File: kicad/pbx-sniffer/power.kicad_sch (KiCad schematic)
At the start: 0 parts

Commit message: add external power circuitry for mcu
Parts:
- added C1: 10u, Capacitor_SMD:C_0603_1608Metric, symbol Device:C_Small
- added C10, C11, C14, C16: 1u, symbol Device:C_Small
- added C12, C13, C15, C17, C18, C19, C3, C4, C5, C6, C7: 100n, symbol Device:C_Small
- added C2: 22u, Capacitor_SMD:C_0603_1608Metric, symbol Device:C_Small
- added C20, C8, C9: 4.7u, symbol Device:C_Small
- added D1: LED_Small, LED_SMD:LED_0805_2012Metric, symbol Device:LED_Small
- added J49: USB_C_Receptacle_USB2.0_14P, Connector_USB:USB_C_Receptacle_GCT_USB4125-xx-x_6P_TopMnt_Horizontal, symbol Connector:USB_C_Receptacle_USB2.0_14P
- added R1: 200, Resistor_SMD:R_0402_1005Metric, symbol Device:R
- added U2: AZ1117CH2-3.3, Package_TO_SOT_SMD:TO-252-2, symbol Regulator_Linear:AZ1117CH2-3.3
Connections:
- new net: D1.2 (A), R1.2
- new net +3V3: C10.1, C11.1, C12.1, C13.1, C14.1, C15.1, C16.1, C17.1, C18.1, C19.1, C2.1, C20.1, C3.1, C4.1, C5.1, C6.1, C7.1, C8.1, R1.1, U2.3 (OUT)
- new net +5V: C1.1, C9.1, J49.A4 (VBUS), J49.A9 (VBUS), J49.B4 (VBUS), J49.B9 (VBUS), U2.1 (IN)
- new net GND: C1.2, C10.2, C11.2, C12.2, C13.2, C14.2, C15.2, C16.2, C17.2, C18.2, C19.2, C2.2, C20.2, C8.2, C9.2, D1.1 (K), J49.A1 (GND), J49.A12 (GND), J49.B1 (GND), J49.B12 (GND), J49.S1 (SHIELD), U2.2 (GND)
- no-connect marks 0 -> 6
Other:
- note added: "3V3 Regulator"
- note added: "MCU USB External Components"
- note added: "MCU VDD External Components"
- note added: "MCU VDDA/VBAT External Components"
- note added: "MCU VDDXSPI1 External Components"
- note added: "USB C Power Input (5V 1A)"

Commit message: add footprints and part numbers for power caps
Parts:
- C10, C11, C14, C16: footprint (none) -> Capacitor_SMD:C_0603_1608Metric; DKPN (none) -> 1276-1946-1-ND
- C12, C13, C15, C17, C18, C19, C3, C4, C5, C6, C7: footprint (none) -> Capacitor_SMD:C_0402_1005Metric; DKPN (none) -> 1276-1043-1-ND
- C20, C8, C9: footprint (none) -> Capacitor_SMD:C_0603_1608Metric; DKPN (none) -> 1276-1044-1-ND
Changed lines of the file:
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@@
 		(rev "v0.1")
 		(company "M5")
-		(comment 4 "Tobe Cynar")
+		(comment 4 "Tobe Cynar, Ian Butler")
+		(comment 5 "Ian Butler")
 	)
 	(rectangle
@@
 			)
 		)
-		(property "Footprint" ""
+		(property "Footprint" "Capacitor_SMD:C_0402_1005Metric"
 			(at 109.22 107.95 0)
 			(effects
@@
 			)
 		)
+		(property "DKPN" "1276-1043-1-ND"
+			(at 109.22 107.95 0)
+			(effects
+				(font
+					(size 1.27 1.27)
+				)
+				(hide yes)
+			)
+		)
 		(pin "1"
 		)
@@
 			)
 		)
-		(property "Footprint" ""
+		(property "Footprint" "Capacitor_SMD:C_0603_1608Metric"
 			(at 64.77 102.87 0)
 			(effects
@@
 			)
 		)
+		(property "DKPN" "1276-1946-1-ND"
+			(at 64.77 102.87 0)
+			(effects
+				(font
+					(size 1.27 1.27)
+				)
+				(hide yes)
+			)
+		)
 		(pin "2"
 		)
@@
 			)
 		)
-		(property "Footprint" ""
+		(property "Footprint" "Capacitor_SMD:C_0603_1608Metric"
 			(at 34.29 102.87 0)
 			(effects
@@
 			)
 		)
+		(property "DKPN" "1276-1946-1-ND"
+			(at 34.29 102.87 0)
+			(effects
+				(font
+					(size 1.27 1.27)
+				)
+				(hide yes)
+			)
+		)
 		(pin "2"
 		)
@@
 			)
 		)
-		(property "Footprint" ""
+		(property "Footprint" "Capacitor_SMD:C_0603_1608Metric"
 			(at 152.4 109.22 0)
 			(effects
@@
 			)
 		)
+		(property "DKPN" "1276-1044-1-ND"
+			(at 152.4 109.22 0)
+			(effects
+				(font
+					(size 1.27 1.27)
+				)
+				(hide yes)
+			)
+		)
 		(pin "2"
 		)
@@
 			)
 		)
-		(property "Footprint" ""
+		(property "Footprint" "Capacitor_SMD:C_0402_1005Metric"
 			(at 55.88 102.87 0)
 			(effects
@@
 			)
 		)
+		(property "DKPN" "1276-1043-1-ND"
+			(at 55.88 102.87 0)
+			(effects
+				(font
+					(size 1.27 1.27)
+				)
+				(hide yes)
+			)
+		)
 		(pin "1"
 		)
@@
 			)
 		)
-		(property "Footprint" ""
+		(property "Footprint" "Capacitor_SMD:C_0402_1005Metric"
 			(at 25.4 138.43 0)
 			(effects
@@
 			)
 		)
+		(property "DKPN" "1276-1043-1-ND"
+			(at 25.4 138.43 0)
+			(effects
+				(font
+					(size 1.27 1.27)
+				)
+				(hide yes)
+			)
+		)
 		(pin "1"
 		)
@@
 			)
 		)
-		(property "Footprint" ""
+		(property "Footprint" "Capacitor_SMD:C_0603_1608Metric"
 			(at 118.11 107.95 0)
 			(effects
@@
 			)
 		)
+		(property "DKPN" "1276-1946-1-ND"
+			(at 118.11 107.95 0)
+			(effects
+				(font
+					(size 1.27 1.27)
+				)
+				(hide yes)
+			)
+		)
 		(pin "2"
 		)
@@
 			)
 		)
-		(property "Footprint" ""
+		(property "Footprint" "Capacitor_SMD:C_0402_1005Metric"
 			(at 43.18 138.43 0)
 			(effects
@@
 			)
 		)
+		(property "DKPN" "1276-1043-1-ND"
+			(at 43.18 138.43 0)
+			(effects
+				(font
+					(size 1.27 1.27)
+				)
+				(hide yes)
+			)
+		)
 		(pin "1"
 		)
@@
 			)
 		)
-		(property "Footprint" ""
+		(property "Footprint" "Capacitor_SMD:C_0402_1005Metric"
 			(at 133.35 72.39 0)
 			(effects
@@
 			)
 		)
+		(property "DKPN" "1276-1043-1-ND"
+			(at 133.35 72.39 0)
+			(effects
+				(font
+					(size 1.27 1.27)
+				)
+				(hide yes)
+			)
+		)
 		(pin "1"
 		)
@@
 			)
 		)
-		(property "Footprint" ""
+		(property "Footprint" "Capacitor_SMD:C_0603_1608Metric"
 			(at 125.73 107.95 0)
 			(effects
@@
 			)
 		)
+		(property "DKPN" "1276-1946-1-ND"
+			(at 125.73 107.95 0)
+			(effects
+				(font
+					(size 1.27 1.27)
+				)
+				(hide yes)
+			)
+		)
 		(pin "2"
 		)
@@
 			)
 		)
-		(property "Footprint" ""
+		(property "Footprint" "Capacitor_SMD:C_0402_1005Metric"
 			(at 115.57 72.39 0)
 			(effects
@@
 			)
 		)
+		(property "DKPN" "1276-1043-1-ND"
+			(at 115.57 72.39 0)
+			(effects
+				(font
+					(size 1.27 1.27)
+				)
+				(hide yes)
+			)
+		)
 		(pin "1"
 		)
@@
 			)
 		)
-		(property "Footprint" ""
+		(property "Footprint" "Capacitor_SMD:C_0402_1005Metric"
 			(at 106.68 72.39 0)
 			(effects
@@
 			)
 		)
+		(property "DKPN" "1276-1043-1-ND"
+			(at 106.68 72.39 0)
+			(effects
+				(font
+					(size 1.27 1.27)
+				)
+				(hide yes)
+			)
+		)
 		(pin "1"
 		)
@@
 			)
 		)
-		(property "Footprint" ""
+		(property "Footprint" "Capacitor_SMD:C_0402_1005Metric"
 			(at 34.29 138.43 0)
 			(effects
@@
 			)
 		)
+		(property "DKPN" "1276-1043-1-ND"
+			(at 34.29 138.43 0)
+			(effects
+				(font
+					(size 1.27 1.27)
+				)
+				(hide yes)
+			)
+		)
 		(pin "1"
 		)
@@
 			)
 		)
-		(property "Footprint" ""
+		(property "Footprint" "Capacitor_SMD:C_0402_1005Metric"
 			(at 124.46 72.39 0)
 			(effects
@@
 			)
 		)
+		(property "DKPN" "1276-1043-1-ND"
+			(at 124.46 72.39 0)
+			(effects
+				(font
+					(size 1.27 1.27)
+				)
+				(hide yes)
+			)
+		)
 		(pin "1"
 		)
@@
 			)
 		)
-		(property "Footprint" ""
+		(property "Footprint" "Capacitor_SMD:C_0603_1608Metric"
 			(at 151.13 72.39 0)
 			(effects
@@
 			)
 		)
+		(property "DKPN" "1276-1044-1-ND"
+			(at 151.13 72.39 0)
+			(effects
+				(font
+					(size 1.27 1.27)
+				)
+				(hide yes)
+			)
+		)
 		(pin "2"
 		)
@@
 			)
 		)
-		(property "Footprint" ""
+		(property "Footprint" "Capacitor_SMD:C_0603_1608Metric"
 			(at 52.07 138.43 0)
 			(effects
@@
 			)
 		)
+		(property "DKPN" "1276-1044-1-ND"
+			(at 52.07 138.43 0)
+			(effects
+				(font
+					(size 1.27 1.27)
+				)
+				(hide yes)
+			)
+		)
 		(pin "1"
 		)
@@
 			)
 		)
-		(property "Footprint" ""
+		(property "Footprint" "Capacitor_SMD:C_0402_1005Metric"
 			(at 142.24 72.39 0)
 			(effects
@@
 			)
 		)
+		(property "DKPN" "1276-1043-1-ND"
+			(at 142.24 72.39 0)
+			(effects
+				(font
+					(size 1.27 1.27)
+				)
+				(hide yes)
+			)
+		)
 		(pin "1"
 		)
@@
 			)
 		)
-		(property "Footprint" ""
+		(property "Footprint" "Capacitor_SMD:C_0402_1005Metric"
 			(at 25.4 102.87 0)
 			(effects
@@
 			(at 25.4 102.87 0)
 			(effects
+				(font
+					(size 1.27 1.27)
+				)
+				(hide yes)
+			)
+		)
+		(property "DKPN" "1276-1043-1-ND"
+			(at 25.4 102.87 0)
+			(effects

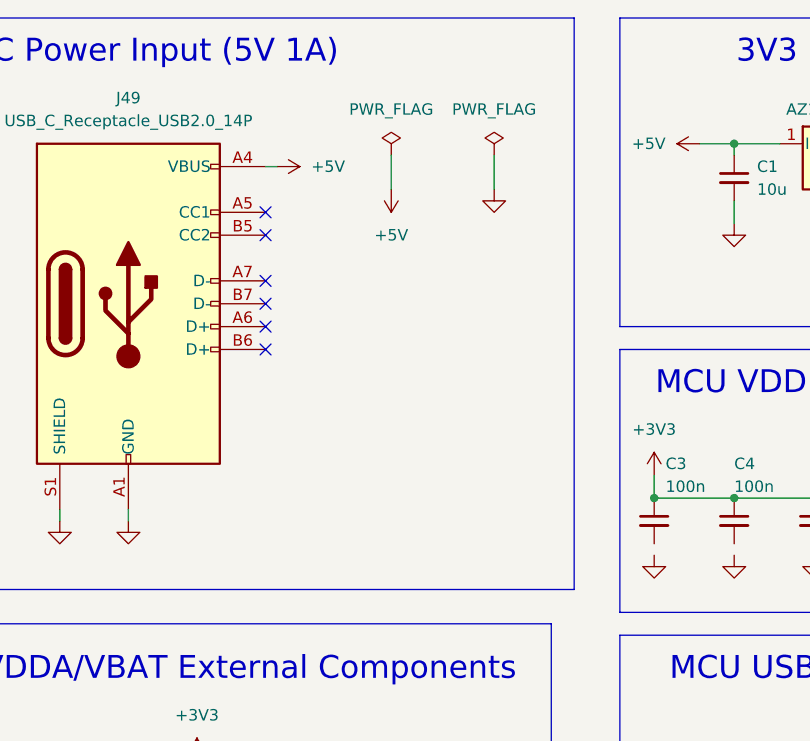
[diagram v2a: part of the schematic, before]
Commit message: add more supporting external circuitry for the MCU
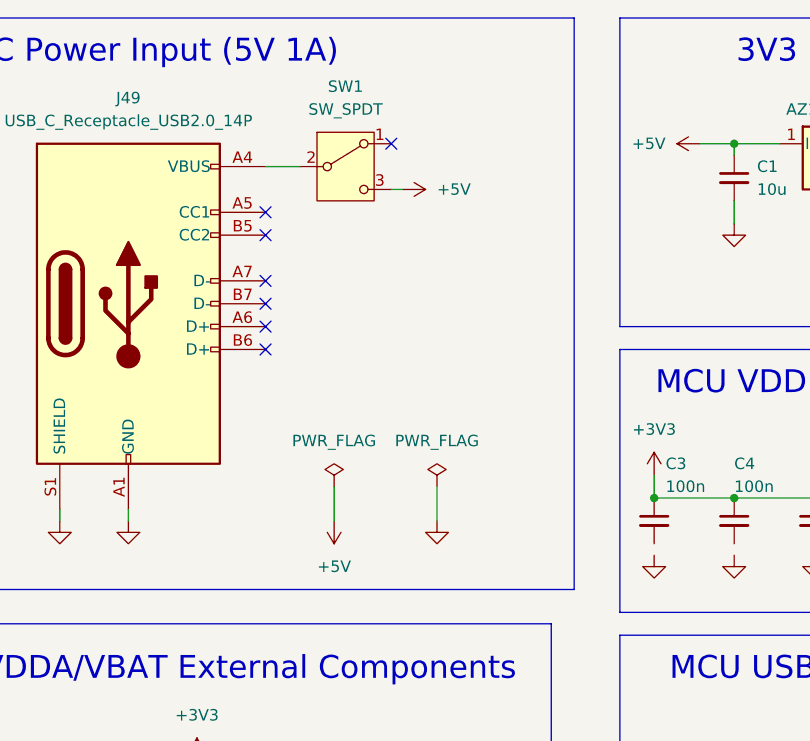
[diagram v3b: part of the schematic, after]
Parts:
- added SW1: SW_SPDT, symbol Switch:SW_SPDT
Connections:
- net +5V: now also SW1.3 (C); no longer J49.A4 (VBUS), J49.A9 (VBUS), J49.B4 (VBUS), J49.B9 (VBUS)
- new net: J49.A4 (VBUS), J49.A9 (VBUS), J49.B4 (VBUS), J49.B9 (VBUS), SW1.2 (B)
- no-connect marks 6 -> 7
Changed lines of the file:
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@@
 	)
 	(no_connect
+		(at 77.47 30.48)
+	)
+	(no_connect
 		(at 63.5 38.1)
 	)
@@
 	(wire
 		(pts
+			(xy 63.5 33.02) (xy 67.31 33.02)
+		)
+		(stroke
+			(width 0)
+			(type default)
+		)
+	)
+	(wire
+		(pts
 			(xy 25.4 140.97) (xy 25.4 142.24)
 		)
@@
 	(wire
 		(pts
-			(xy 63.5 33.02) (xy 64.77 33.02)
+			(xy 77.47 35.56) (xy 78.74 35.56)
 		)
 		(stroke
@@
 	(wire
 		(pts
-			(xy 88.9 31.75) (xy 88.9 35.56)
+			(xy 82.55 68.58) (xy 82.55 72.39)
 		)
 		(stroke
@@
 	(wire
 		(pts
-			(xy 77.47 31.75) (xy 77.47 35.56)
+			(xy 71.12 68.58) (xy 71.12 72.39)
 		)
 		(stroke
@@
 	(symbol
 		(lib_id "power:PWR_FLAG")
-		(at 88.9 31.75 0)
+		(at 82.55 68.58 0)
 		(unit 1)
 		(exclude_from_sim no)
@@
 		(fields_autoplaced yes)
 		(property "Reference" "#FLG02"
-			(at 88.9 29.845 0)
+			(at 82.55 66.675 0)
 			(effects
 				(font
@@
 		)
 		(property "Value" "PWR_FLAG"
-			(at 88.9 26.67 0)
+			(at 82.55 63.5 0)
 			(effects
 				(font
@@
 		)
 		(property "Footprint" ""
-			(at 88.9 31.75 0)
+			(at 82.55 68.58 0)
 			(effects
 				(font
@@
 		)
 		(property "Datasheet" "~"
-			(at 88.9 31.75 0)
+			(at 82.55 68.58 0)
 			(effects
 				(font
@@
 		)
 		(property "Description" "Special symbol for telling ERC where power comes from"
-			(at 88.9 31.75 0)
+			(at 82.55 68.58 0)
 			(effects
 				(font
@@
 	(symbol
 		(lib_id "power:+5V")
-		(at 77.47 35.56 180)
+		(at 71.12 72.39 180)
 		(unit 1)
 		(exclude_from_sim no)
@@
 		(fields_autoplaced yes)
 		(property "Reference" "#PWR03"
-			(at 77.47 31.75 0)
+			(at 71.12 68.58 0)
 			(effects
 				(font
@@
 		)
 		(property "Value" "+5V"
-			(at 77.47 40.64 0)
+			(at 71.12 77.47 0)
 			(effects
 				(font
@@
 		)
 		(property "Footprint" ""
-			(at 77.47 35.56 0)
+			(at 71.12 72.39 0)
 			(effects
 				(font
@@
 		)
 		(property "Datasheet" ""
-			(at 77.47 35.56 0)
+			(at 71.12 72.39 0)
 			(effects
 				(font
@@
 		)
 		(property "Description" "Power symbol creates a global label with name \"+5V\""
-			(at 77.47 35.56 0)
+			(at 71.12 72.39 0)
 			(effects
 				(font
@@
 	)
 	(symbol
+		(lib_id "Switch:SW_SPDT")
+		(at 72.39 33.02 0)
+		(unit 1)
+		(exclude_from_sim no)
+		(in_bom yes)
+		(on_board yes)
+		(dnp no)
+		(fields_autoplaced yes)
+		(property "Reference" "SW1"
+			(at 72.39 24.13 0)
+			(effects
+				(font
+					(size 1.27 1.27)
+				)
+			)
+		)
+		(property "Value" "SW_SPDT"
+			(at 72.39 26.67 0)
+			(effects
+				(font
+					(size 1.27 1.27)
+				)
+			)
+		)
+		(property "Footprint" ""
+			(at 72.39 33.02 0)
+			(effects
+				(font
+					(size 1.27 1.27)
+				)
+				(hide yes)
+			)
+		)
+		(property "Datasheet" "~"
+			(at 72.39 40.64 0)
+			(effects
+				(font
+					(size 1.27 1.27)
+				)
+				(hide yes)
+			)
+		)
+		(property "Description" "Switch, single pole double throw"
+			(at 72.39 33.02 0)
+			(effects
+				(font
+					(size 1.27 1.27)
+				)
+				(hide yes)
+			)
+		)
+		(property "DKPN" "2449-ANT11SECQE-ND"
+			(at 72.39 33.02 0)
+			(effects
+				(font
+					(size 1.27 1.27)
+				)
+				(hide yes)
+			)
+		)
+		(pin "3"
+		)
+		(pin "1"
+		)
+		(pin "2"
+		)
+		(instances
+			(project ""
+				(path "/4a5b9b8a-323a-4796-bf73-ccba532d2e31/5440b238-ad38-4f50-b001-ed881622e44b"
+					(reference "SW1")
+					(unit 1)
+				)
+			)
+		)
+	)
+	(symbol
 		(lib_id "power:GND")
 		(at 55.88 106.68 0)
@@
 	(symbol
 		(lib_id "power:+5V")
-		(at 64.77 33.02 270)
+		(at 78.74 35.56 270)
 		(unit 1)
 		(exclude_from_sim no)
@@
 		(fields_autoplaced yes)
 		(property "Reference" "#PWR01"
-			(at 60.96 33.02 0)
+			(at 74.93 35.56 0)
 			(effects
 				(font
@@
 		)
 		(property "Value" "+5V"
-			(at 68.58 33.0199 90)
+			(at 82.55 35.5599 90)
 			(effects
 				(font
@@
 		)
 		(property "Footprint" ""
-			(at 64.77 33.02 0)
+			(at 78.74 35.56 0)
 			(effects
 				(font
@@
 		)
 		(property "Datasheet" ""
-			(at 64.77 33.02 0)
+			(at 78.74 35.56 0)
 			(effects
 				(font
@@
 		)
 		(property "Description" "Power symbol creates a global label with name \"+5V\""
-			(at 64.77 33.02 0)
+			(at 78.74 35.56 0)
 			(effects
 				(font
@@
 	(symbol
 		(lib_id "power:PWR_FLAG")
-		(at 77.47 31.75 0)
+		(at 71.12 68.58 0)
 		(unit 1)
 		(exclude_from_sim no)
@@
 		(fields_autoplaced yes)
 		(property "Reference" "#FLG01"
-			(at 77.47 29.845 0)
+			(at 71.12 66.675 0)
 			(effects
 				(font
@@
 		)
 		(property "Value" "PWR_FLAG"
-			(at 77.47 26.67 0)
+			(at 71.12 63.5 0)
 			(effects
 				(font
@@
 		)
 		(property "Footprint" ""
-			(at 77.47 31.75 0)
+			(at 71.12 68.58 0)
 			(effects
 				(font
@@
 		)
 		(property "Datasheet" "~"
-			(at 77.47 31.75 0)
+			(at 71.12 68.58 0)
 			(effects
 				(font
@@
 		)
 		(property "Description" "Special symbol for telling ERC where power comes from"
-			(at 77.47 31.75 0)
+			(at 71.12 68.58 0)
 			(effects
 				(font
@@
 	(symbol
 		(lib_id "power:GND")
-		(at 88.9 35.56 0)
+		(at 82.55 72.39 0)
 		(unit 1)
 		(exclude_from_sim no)
@@
 		(fields_autoplaced yes)
 		(property "Reference" "#PWR04"
-			(at 88.9 41.91 0)
+			(at 82.55 78.74 0)
 			(effects
 				(font
@@
 		)
 		(property "Value" "GND"
-			(at 88.9 40.64 0)
+			(at 82.55 77.47 0)
 			(effects
 				(font
@@
 		)
 		(property "Footprint" ""
-			(at 88.9 35.56 0)
+			(at 82.55 72.39 0)
 			(effects
 				(font
@@
 		)
 		(property "Datasheet" ""
-			(at 88.9 35.56 0)
+			(at 82.55 72.39 0)
 			(effects
 				(font
@@
 		)
 		(property "Description" "Power symbol creates a global label with name \"GND\" , ground"
-			(at 88.9 35.56 0)
+			(at 82.55 72.39 0)
 			(effects
 				(font

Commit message: commenced placement on pcb
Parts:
- renumbered C13 to C1, C12 to C10, C1 to C11, C4 to C12, C10 to C13, C5 to C14, C11 to C15, C6 to C16, C2 to C17, C7 to C18, C8 to C19, C17 to C2, C9 to C20, C14 to C3, C18 to C4, C19 to C5, C20 to C6, C15 to C7, C16 to C8, C3 to C9
